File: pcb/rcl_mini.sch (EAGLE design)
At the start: 60 parts, among them CN1 USB mini B, Q1 8MHz, Q2 IRLML5203, U1 MCP6002T-I/SN, U2 MCP6002T-I/SN, U3 MCP6002T-I/SN, U4 STM32F100CBT6, U5 MCP73831/OT, U6 MCP1703CB, X1 BAT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

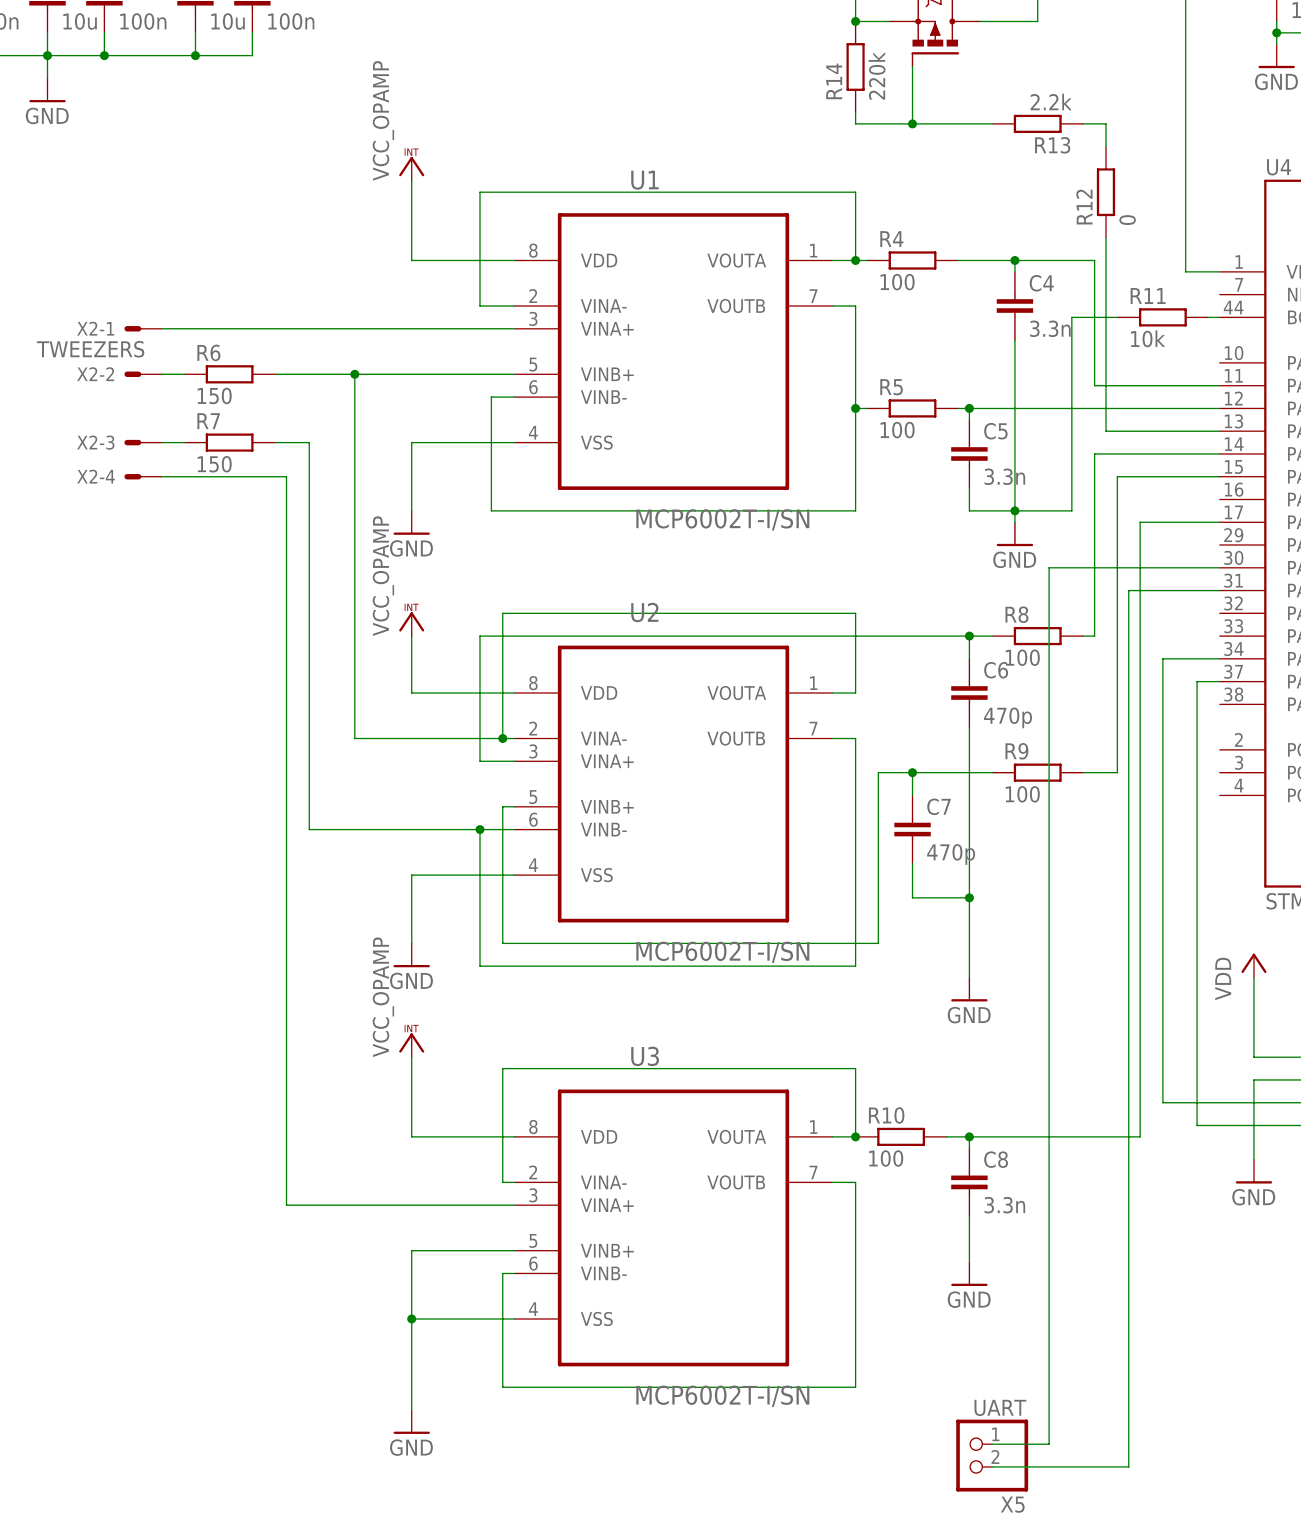
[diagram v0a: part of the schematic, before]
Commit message: mcp6002 package was changed from msop to soic
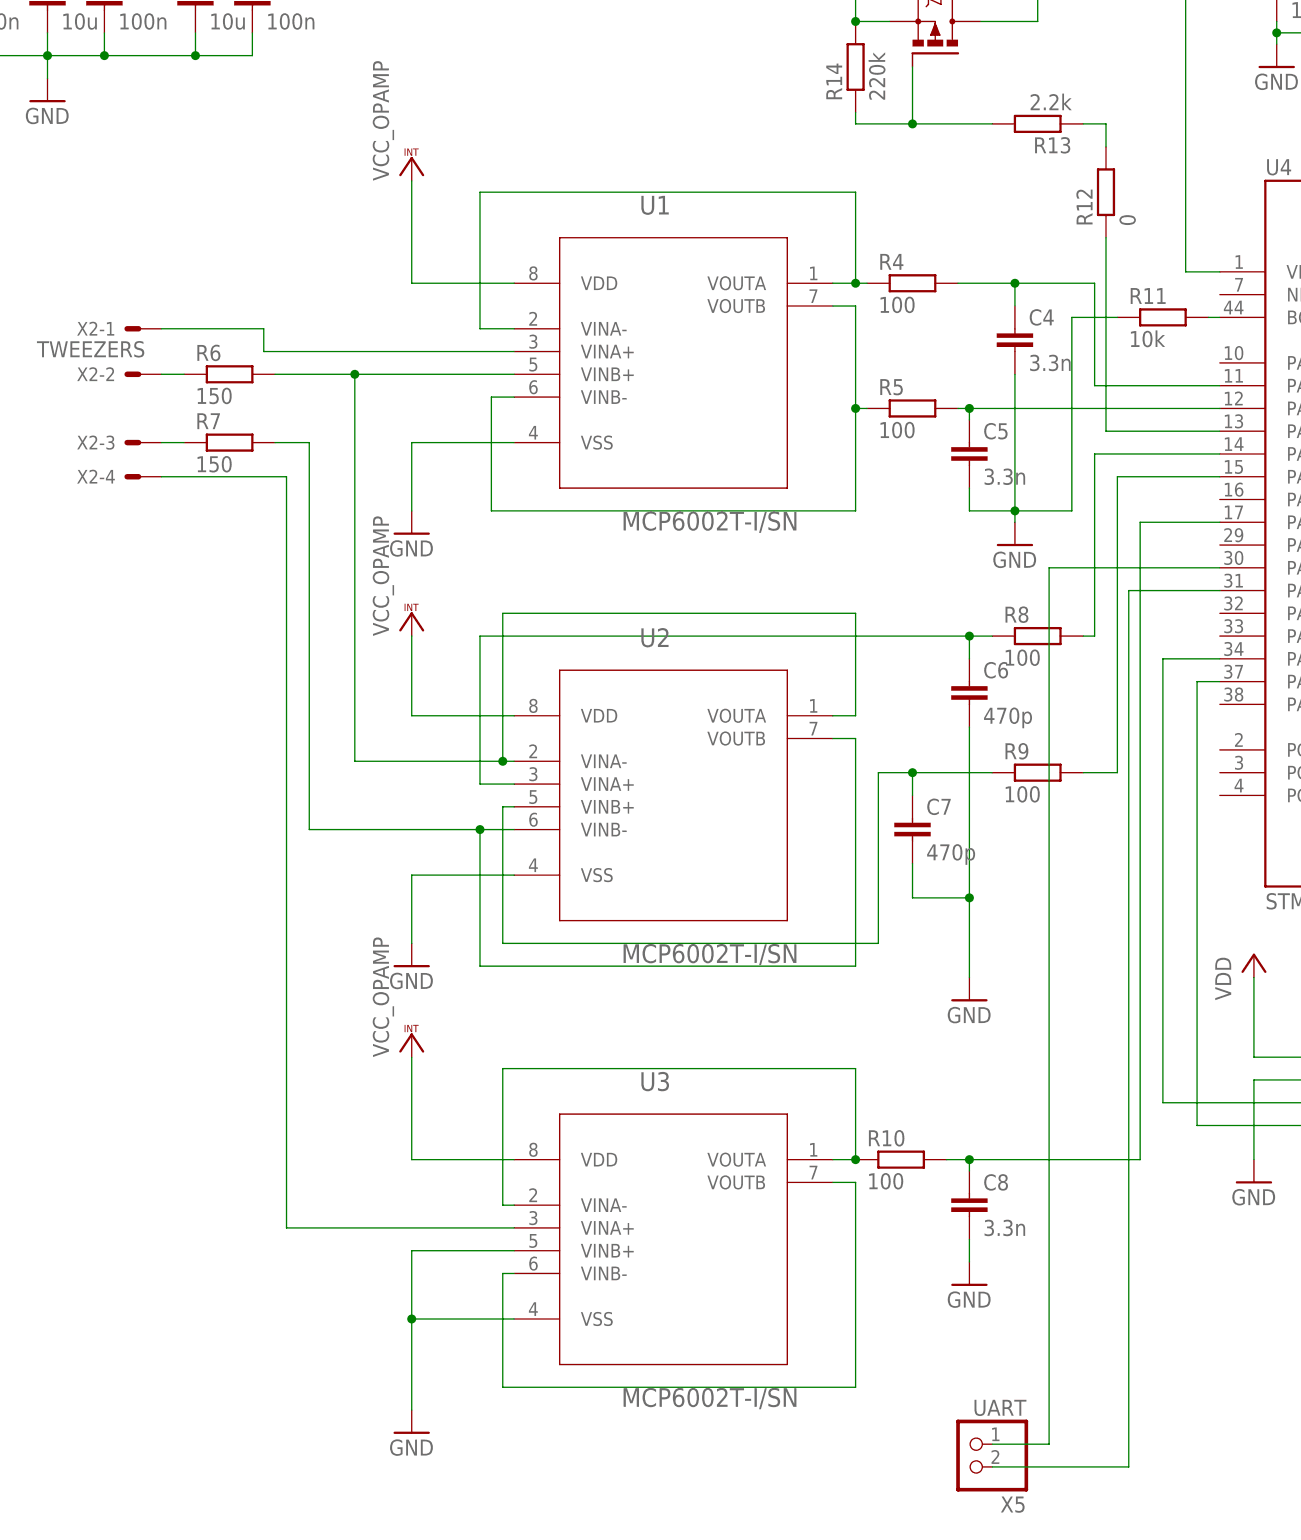
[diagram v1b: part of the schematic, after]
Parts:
- U1, U2, U3: device MCP6002T:MCP6002T-I/MS -> MCP6002:MCP6002-E/SN
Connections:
- net LPOT renamed N$7
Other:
- moved on the sheet: C4, C8, R10, R4, U1, U2, U3
